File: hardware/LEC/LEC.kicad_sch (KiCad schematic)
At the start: 37 parts, among them J1 54-00278, J10 Conn_01x02, J11 54-00278, J12 54-00278, J13 54-00278, J14 54-00278, J2 54-00278, J3 54-00278, J4 54-00278, J5 54-00278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

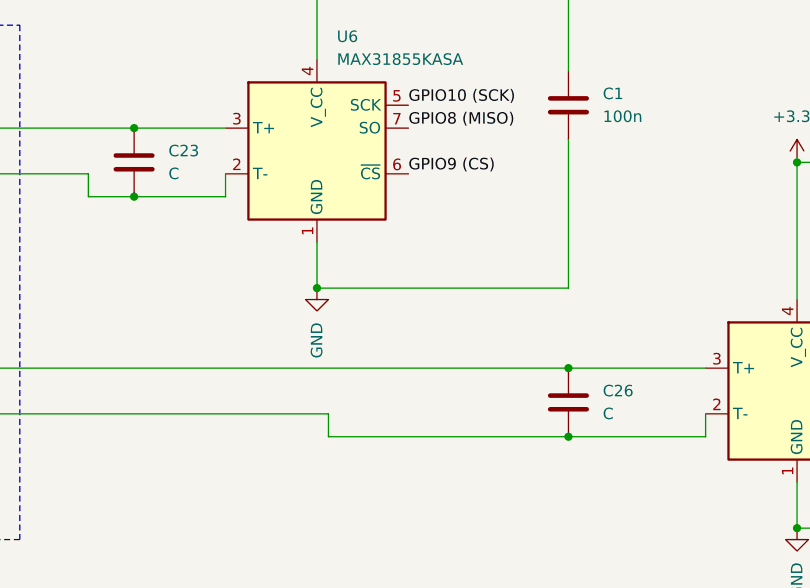
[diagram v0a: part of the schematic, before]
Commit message: Updated schematic documentation, more production files
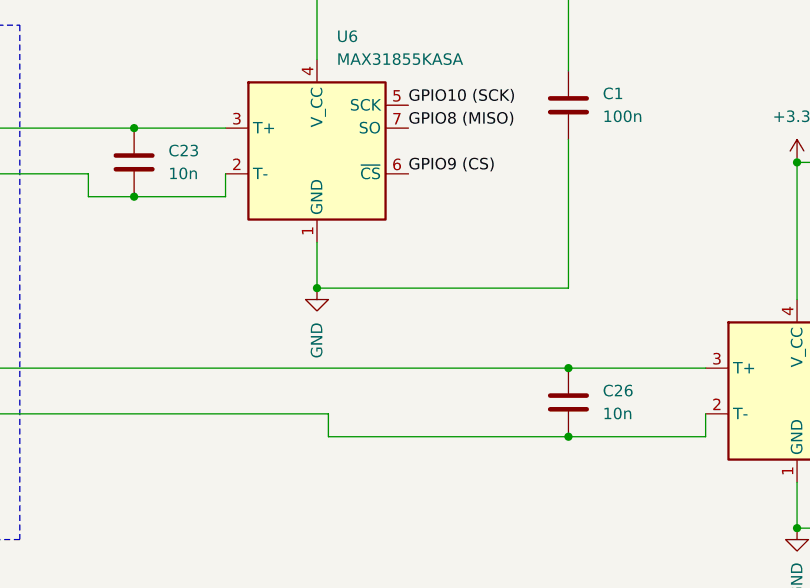
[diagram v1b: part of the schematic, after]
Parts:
- C1: DigiKey (none) -> https://www.digikey.com/en/products/detail/samsung-electro-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; Digikey https://www.digikey.com/en/products/detail/samsung-electro-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 -> (none)
- C23, C26: value C -> 10n
- D1: DigiKey (none) -> https://www.digikey.com/en/products/detail/vishay-general-s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
- R3: DigiKey (none) -> https://www.digikey.com/en/products/detail/vishay-dale/TNPW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; Digikey https://www.digikey.com/en/products/detail/vishay-dale/TNPW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 -> (none)
- U15: DigiKey (none) -> https://www.digikey.com/en/products/detail/microchip-techno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; Digikey https://www.digikey.com/en/products/detail/microchip-techno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 -> (none)
- U3: DigiKey (none) -> https://www.digikey.com/en/products/detail/onsemi/MC7809CTG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; Digikey https://www.digikey.com/en/products/detail/onsemi/MC7809CTG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 -> (none)
- U4: DigiKey (none) -> https://www.digikey.com/en/products/detail/winbond-electron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; Digikey https://www.digikey.com/en/products/detail/winbond-electron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 -> (none)
- U5, U6: DigiKey (none) -> https://www.digikey.com/en/products/detail/analog-devices-i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
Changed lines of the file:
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@@
       (effects (font (size 1.27 1.27)) hide)
     )
-    (property "Digikey" "https://www.digikey.com/en/products/detail/vishay-dale/TNPW060310K0BEEA/1606881" (at 345.44 171.45 0)
+    (property "DigiKey" "https://www.digikey.com/en/products/detail/vishay-dale/TNPW060310K0BEEA/1606881" (at 345.44 171.45 0)
       (effects (font (size 1.27 1.27)) hide)
     )
@@
       (effects (font (size 1.27 1.27) italic) hide)
     )
-    (property "Digikey" "https://www.digikey.com/en/products/detail/winbond-electronics/W25Q128JVSIQ/5803943" (at 342.9 229.87 0)
+    (property "DigiKey" "https://www.digikey.com/en/products/detail/winbond-electronics/W25Q128JVSIQ/5803943" (at 342.9 229.87 0)
       (effects (font (size 1.27 1.27)) hide)
     )
@@
       (effects (font (size 1.27 1.27)) hide)
     )
-    (property "Digikey" "https://www.digikey.com/en/products/detail/samsung-electro-mechanics/CL10B104KB8NNNC/3886658" (at 181.61 254 0)
+    (property "DigiKey" "https://www.digikey.com/en/products/detail/samsung-electro-mechanics/CL10B104KB8NNNC/3886658" (at 181.61 254 0)
       (effects (font (size 1.27 1.27)) hide)
     )
@@
       (effects (font (size 1.27 1.27)) hide)
     )
-    (property "Digikey" "https://www.digikey.com/en/products/detail/samsung-electro-mechanics/CL10B104KB8NNNC/3886658" (at 247.65 240.03 0)
+    (property "DigiKey" "https://www.digikey.com/en/products/detail/samsung-electro-mechanics/CL10B104KB8NNNC/3886658" (at 247.65 240.03 0)
       (effects (font (size 1.27 1.27)) hide)
     )
@@
       (effects (font (size 1.27 1.27)) hide)
     )
+    (property "DigiKey" "https://www.digikey.com/en/products/detail/vishay-general-semiconductor-diodes-division/1N5817-E3-73/2139978" (at 321.31 129.54 90)
+      (effects (font (size 1.27 1.27)) hide)
+    )
     (pin "1")
     (pin "2")
@@
     )
     (property "Datasheet" "http://datasheets.maximintegrated.com/en/ds/MAX31855.pdf" (at 99.06 229.87 0)
+      (effects (font (size 1.27 1.27)) hide)
+    )
+    (property "DigiKey" "https://www.digikey.com/en/products/detail/analog-devices-inc-maxim-integrated/MAX31855KASA/2591564" (at 99.06 229.87 0)
       (effects (font (size 1.27 1.27)) hide)
     )
@@
       (effects (font (size 1.27 1.27)) hide)
     )
-    (property "Digikey" "https://www.digikey.com/en/products/detail/vishay-dale/TNPW060310K0BEEA/1606881" (at 345.44 201.93 0)
+    (property "DigiKey" "https://www.digikey.com/en/products/detail/vishay-dale/TNPW060310K0BEEA/1606881" (at 345.44 201.93 0)
       (effects (font (size 1.27 1.27)) hide)
     )
@@
       (effects (font (size 1.27 1.27) italic) hide)
     )
-    (property "Digikey" "https://www.digikey.com/en/products/detail/onsemi/MC7809CTG/1481254" (at 194.31 58.42 0)
+    (property "DigiKey" "https://www.digikey.com/en/products/detail/onsemi/MC7809CTG/1481254" (at 194.31 58.42 0)
       (effects (font (size 1.27 1.27)) hide)
     )
@@
       (effects (font (size 1.27 1.27)) hide)
     )
-    (property "Digikey" "https://www.digikey.com/en/products/detail/samsung-electro-mechanics/CL10B104KB8NNNC/3886658" (at 127 224.79 0)
+    (property "DigiKey" "https://www.digikey.com/en/products/detail/samsung-electro-mechanics/CL10B104KB8NNNC/3886658" (at 127 224.79 0)
       (effects (font (size 1.27 1.27)) hide)
     )
@@
       (effects (font (size 1.27 1.27)) (justify left))
     )
-    (property "Value" "C" (at 82.55 232.41 0)
+    (property "Value" "10n" (at 82.55 232.41 0)
       (effects (font (size 1.27 1.27)) (justify left))
     )
@@
       (effects (font (size 1.27 1.27) italic) hide)
     )
-    (property "Digikey" "https://www.digikey.com/en/products/detail/microchip-technology/MCP3564RT-E-ST/12807301?s=N4IgTCBcDaILIGEAKBmArANgCwCUAqAtAKID0AyniALoC%2BQA" (at 144.78 156.21 0)
+    (property "DigiKey" "https://www.digikey.com/en/products/detail/microchip-technology/MCP3564RT-E-ST/12807301?s=N4IgTCBcDaILIGEAKBmArANgCwCUAqAtAKID0AyniALoC%2BQA" (at 144.78 156.21 0)
       (effects (font (size 1.27 1.27)) hide)
     )
@@
       (effects (font (size 1.27 1.27)) (justify left))
     )
-    (property "Value" "C" (at 130.81 259.08 0)
+    (property "Value" "10n" (at 130.81 259.08 0)
       (effects (font (size 1.27 1.27)) (justify left))
     )
@@
       (effects (font (size 1.27 1.27)) hide)
     )
+    (property "DigiKey" "https://www.digikey.com/en/products/detail/analog-devices-inc-maxim-integrated/MAX31855KASA/2591564" (at 152.4 256.54 0)
+      (effects (font (size 1.27 1.27)) hide)
+    )
